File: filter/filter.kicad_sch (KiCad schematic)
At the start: 38 parts, among them Q1 PNP, Q2 PNP, SW1 High Pass / Low Pass, U1 LM13700, U2 TL074, U3 TL072

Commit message: Experiment with pcb
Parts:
- C1, C2, C3, C4, C5, C6: footprint (none) -> Capacitor_THT:C_Disc_D5.0mm_W2.5mm_P2.50mm
- CVLevel1: renamed from CVLevel; footprint (none) -> Potentiometer_THT:Potentiometer_Piher_T-16H_Single_Horizontal
- Cutoff1: renamed from Cutoff; footprint (none) -> Potentiometer_THT:Potentiometer_Piher_T-16H_Single_Horizontal
- D1, D2: footprint (none) -> LED_THT:LED_D5.0mm
- Q1, Q2: footprint (none) -> Package_TO_SOT_THT:TO-92
- R1, R10, R11, R12, R13, R14, R15, R16, R18, R19, R2, R20, R21, R3, R4, R5, R6, R7, R8, R9: footprint (none) -> Resistor_THT:R_Axial_DIN0207_L6.3mm_D2.5mm_P10.16mm_Horizontal
- R17: footprint (none) -> Resistor_THT:R_Axial_DIN0207_L6.3mm_D2.5mm_P2.54mm_Vertical
- Resonance1: renamed from Resonance; footprint (none) -> Potentiometer_THT:Potentiometer_Piher_T-16L_Single_Vertical_Hole
- U1: footprint (none) -> Package_DIP:DIP-16_W7.62mm
- U2: footprint (none) -> Package_DIP:DIP-14_W7.62mm
- U3: footprint (none) -> Package_DIP:DIP-8_W7.62mm
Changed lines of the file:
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@@
 			)
 		)
-		(property "Footprint" ""
+		(property "Footprint" "Resistor_THT:R_Axial_DIN0207_L6.3mm_D2.5mm_P10.16mm_Horizontal"
 			(at 130.556 167.386 90)
 			(effects
@@
 			)
 		)
-		(property "Footprint" ""
+		(property "Footprint" "Package_TO_SOT_THT:TO-92"
 			(at 229.87 82.55 0)
 			(effects
@@
 			)
 		)
-		(property "Footprint" ""
+		(property "Footprint" "Resistor_THT:R_Axial_DIN0207_L6.3mm_D2.5mm_P10.16mm_Horizontal"
 			(at 115.316 167.894 90)
 			(effects
@@
 			)
 		)
-		(property "Footprint" ""
+		(property "Footprint" "Resistor_THT:R_Axial_DIN0207_L6.3mm_D2.5mm_P10.16mm_Horizontal"
 			(at 138.176 72.136 90)
 			(effects
@@
 			)
 		)
-		(property "Footprint" ""
+		(property "Footprint" "Capacitor_THT:C_Disc_D5.0mm_W2.5mm_P2.50mm"
 			(at 29.21 120.65 0)
 			(effects
@@
 			)
 		)
-		(property "Footprint" ""
+		(property "Footprint" "Package_DIP:DIP-16_W7.62mm"
 			(at 33.655 60.96 0)
 			(effects
@@
 			)
 		)
-		(property "Footprint" ""
+		(property "Footprint" "Package_DIP:DIP-8_W7.62mm"
 			(at 25.4 185.42 0)
 			(effects
@@
 			)
 		)
-		(property "Footprint" ""
+		(property "Footprint" "Resistor_THT:R_Axial_DIN0207_L6.3mm_D2.5mm_P10.16mm_Horizontal"
 			(at 115.316 145.034 90)
 			(effects
@@
 			)
 		)
-		(property "Footprint" ""
+		(property "Footprint" "Package_DIP:DIP-8_W7.62mm"
 			(at 33.02 138.43 0)
 			(effects
@@
 			)
 		)
-		(property "Footprint" ""
+		(property "Footprint" "Resistor_THT:R_Axial_DIN0207_L6.3mm_D2.5mm_P10.16mm_Horizontal"
 			(at 81.3435 85.7885 90)
 			(effects
@@
 			)
 		)
-		(property "Footprint" ""
+		(property "Footprint" "Resistor_THT:R_Axial_DIN0207_L6.3mm_D2.5mm_P10.16mm_Horizontal"
 			(at 220.726 106.426 90)
 			(effects
@@
 			)
 		)
-		(property "Footprint" ""
+		(property "Footprint" "Package_DIP:DIP-16_W7.62mm"
 			(at 204.47 55.245 0)
 			(effects
@@
 			)
 		)
-		(property "Footprint" ""
+		(property "Footprint" "Resistor_THT:R_Axial_DIN0207_L6.3mm_D2.5mm_P10.16mm_Horizontal"
 			(at 192.024 66.294 90)
 			(effects
@@
 		(exclude_from_sim no)
 		(in_bom yes)
-		(on_board yes)
+		(on_board no)
 		(dnp no)
 		(property "Reference" "R17"
@@
 			)
 		)
-		(property "Footprint" ""
+		(property "Footprint" "Resistor_THT:R_Axial_DIN0207_L6.3mm_D2.5mm_P2.54mm_Vertical"
 			(at 73.406 48.006 90)
 			(effects
@@
 			)
 		)
-		(property "Footprint" ""
+		(property "Footprint" "Capacitor_THT:C_Disc_D5.0mm_W2.5mm_P2.50mm"
 			(at 39.37 120.65 0)
 			(effects
@@
 		(exclude_from_sim no)
 		(in_bom yes)
-		(on_board yes)
+		(on_board no)
 		(dnp no)
-		(property "Reference" "Resonance"
+		(property "Reference" "Resonance1"
 			(at 113.792 40.64 90)
 			(effects
@@
 			)
 		)
-		(property "Footprint" ""
+		(property "Footprint" "Potentiometer_THT:Potentiometer_Piher_T-16L_Single_Vertical_Hole"
 			(at 118.11 44.45 0)
 			(effects
@@
 			(project "low-pass-filter"
 				(path "/e72ee090-6f9b-4823-9ab6-f31beee51bd1"
-					(reference "Resonance")
+					(reference "Resonance1")
 					(unit 1)
 				)
@@
 			)
 		)
-		(property "Footprint" ""
+		(property "Footprint" "Resistor_THT:R_Axial_DIN0207_L6.3mm_D2.5mm_P10.16mm_Horizontal"
 			(at 260.604 114.554 90)
 			(effects
@@
 			)
 		)
-		(property "Footprint" ""
+		(property "Footprint" "Capacitor_THT:C_Disc_D5.0mm_W2.5mm_P2.50mm"
 			(at 243.84 95.25 0)
 			(effects
@@
 			)
 		)
-		(property "Footprint" ""
+		(property "Footprint" "Capacitor_THT:C_Disc_D5.0mm_W2.5mm_P2.50mm"
 			(at 237.49 40.64 0)
 			(effects
@@
 			)
 		)
-		(property "Footprint" ""
+		(property "Footprint" "LED_THT:LED_D5.0mm"
 			(at 137.16 97.79 0)
 			(effects
@@
 			)
 		)
-		(property "Footprint" ""
+		(property "Footprint" "Resistor_THT:R_Axial_DIN0207_L6.3mm_D2.5mm_P10.16mm_Horizontal"
 			(at 233.934 141.986 90)
 			(effects
@@
 			)
 		)
-		(property "Footprint" ""
+		(property "Footprint" "Resistor_THT:R_Axial_DIN0207_L6.3mm_D2.5mm_P10.16mm_Horizontal"
 			(at 192.024 43.434 90)
 			(effects
@@
 			)
 		)
-		(property "Footprint" ""
+		(property "Footprint" "Resistor_THT:R_Axial_DIN0207_L6.3mm_D2.5mm_P10.16mm_Horizontal"
 			(at 220.726 123.444 90)
 			(effects
@@
 			)
 		)
-		(property "Footprint" ""
+		(property "Footprint" "Package_DIP:DIP-14_W7.62mm"
 			(at 207.01 27.94 0)
 			(effects
@@
 			)
 		)
-		(property "Footprint" ""
+		(property "Footprint" "Package_DIP:DIP-14_W7.62mm"
 			(at 245.11 81.28 0)
 			(effects
@@
 			)
 		)
-		(property "Footprint" ""
+		(property "Footprint" "Resistor_THT:R_Axial_DIN0207_L6.3mm_D2.5mm_P10.16mm_Horizontal"
 			(at 242.824 147.574 90)
 			(effects
@@
 			)
 		)
-		(property "Footprint" ""
+		(property "Footprint" "Resistor_THT:R_Axial_DIN0207_L6.3mm_D2.5mm_P10.16mm_Horizontal"
 			(at 105.156 155.956 90)
 			(effects
@@
 			)
 		)
-		(property "Footprint" ""
+		(property "Footprint" "Resistor_THT:R_Axial_DIN0207_L6.3mm_D2.5mm_P10.16mm_Horizontal"
 			(at 235.204 106.426 90)
 			(effects
@@
 		(exclude_from_sim no)
 		(in_bom yes)
-		(on_board yes)
+		(on_board no)
 		(dnp no)
-		(property "Reference" "CVLevel"
+		(property "Reference" "CVLevel1"
 			(at 212.598 139.7 0)
 			(effects
@@
 			)
 		)
-		(property "Footprint" ""
+		(property "Footprint" "Potentiometer_THT:Potentiometer_Piher_T-16H_Single_Horizontal"
 			(at 214.63 140.97 0)
 			(effects
@@
 			(project "low-pass-filter"
 				(path "/e72ee090-6f9b-4823-9ab6-f31beee51bd1"
-					(reference "CVLevel")
+					(reference "CVLevel1")
 					(unit 1)
 				)
@@
 			)
 		)
-		(property "Footprint" ""
+		(property "Footprint" "Capacitor_THT:C_Disc_D5.0mm_W2.5mm_P2.50mm"
 			(at 154.94 44.45 0)
 			(effects
@@
 			)
 		)
-		(property "Footprint" ""
+		(property "Footprint" "Package_DIP:DIP-16_W7.62mm"
 			(at 29.21 84.455 0)
 			(effects
@@
 		(exclude_from_sim no)
 		(in_bom yes)
-		(on_board yes)
+		(on_board no)
 		(dnp no)
 		(fields_autoplaced yes)
@@
 		(exclude_from_sim no)
 		(in_bom yes)
-		(on_board yes)
+		(on_board no)
 		(dnp no)
-		(property "Reference" "Cutoff"
+		(property "Reference" "Cutoff1"
 			(at 243.84 159.258 90)
 			(effects
@@
 			)
 		)
-		(property "Footprint" ""
+		(property "Footprint" "Potentiometer_THT:Potentiometer_Piher_T-16H_Single_Horizontal"
 			(at 243.84 156.21 0)
 			(effects
@@
 			(project "low-pass-filter"
 				(path "/e72ee090-6f9b-4823-9ab6-f31beee51bd1"
-					(reference "Cutoff")
+					(reference "Cutoff1")
 					(unit 1)
 				)
@@
 			)
 		)
-		(property "Footprint" ""
+		(property "Footprint" "Package_DIP:DIP-14_W7.62mm"
 			(at 30.48 49.53 0)
 			(effects
@@
 			)
 		)
-		(property "Footprint" ""
+		(property "Footprint" "Resistor_THT:R_Axial_DIN0207_L6.3mm_D2.5mm_P10.16mm_Horizontal"
 			(at 98.806 98.044 90)
 			(effects
@@
 			)
 		)
-		(property "Footprint" ""
+		(property "Footprint" "Package_DIP:DIP-14_W7.62mm"
 			(at 134.62 130.81 0)
 			(effects
@@
 			)
 		)
-		(property "Footprint" ""
+		(property "Footprint" "Package_DIP:DIP-16_W7.62mm"
 			(at 29.21 103.505 0)
 			(effects
@@
 			)
 		)
-		(property "Footprint" ""
+		(property "Footprint" "Package_DIP:DIP-8_W7.62mm"
 			(at 82.55 93.98 0)
 			(effects
@@
 			)
 		)
-		(property "Footprint" ""
+		(property "Footprint" "Package_TO_SOT_THT:TO-92"
 			(at 243.84 82.55 0)
 			(effects
@@
 			)
 		)
-		(property "Footprint" ""
+		(property "Footprint" "Resistor_THT:R_Axial_DIN0207_L6.3mm_D2.5mm_P10.16mm_Horizontal"
 			(at 176.276 45.466 90)
 			(effects
@@
 			)
 		)
-		(property "Footprint" ""
+		(property "Footprint" "Package_DIP:DIP-14_W7.62mm"
 			(at 139.7 53.34 0)
 			(effects
@@
 			)
 		)
-		(property "Footprint" ""
+		(property "Footprint" "LED_THT:LED_D5.0mm"
 			(at 138.43 83.82 0)
 			(effects
@@
 			)
 		)
-		(property "Footprint" ""
+		(property "Footprint" "Package_DIP:DIP-16_W7.62mm"
 			(at 129.54 156.845 0)
 			(effects
@@
 			)
 		)
-		(property "Footprint" ""
+		(property "Footprint" "Resistor_THT:R_Axial_DIN0207_L6.3mm_D2.5mm_P10.16mm_Horizontal"
 			(at 176.784 66.294 90)
 			(effects
@@
 			)
 		)
-		(property "Footprint" ""
+		(property "Footprint" "Capacitor_THT:C_Disc_D5.0mm_W2.5mm_P2.50mm"
 			(at 149.86 104.14 0)
 			(effects
@@
 			)
 		)
-		(property "Footprint" ""
+		(property "Footprint" "Resistor_THT:R_Axial_DIN0207_L6.3mm_D2.5mm_P10.16mm_Horizontal"
 			(at 98.806 85.344 90)
 			(effects
@@
 			)
 		)
-		(property "Footprint" ""
+		(property "Footprint" "Resistor_THT:R_Axial_DIN0207_L6.3mm_D2.5mm_P10.16mm_Horizontal"
 			(at 252.476 139.954 90)
 			(effects
@@
 			)
 		)
-		(property "Footprint" ""
+		(property "Footprint" "Resistor_THT:R_Axial_DIN0207_L6.3mm_D2.5mm_P10.16mm_Horizontal"
 			(at 119.126 59.436 90)
 			(effects

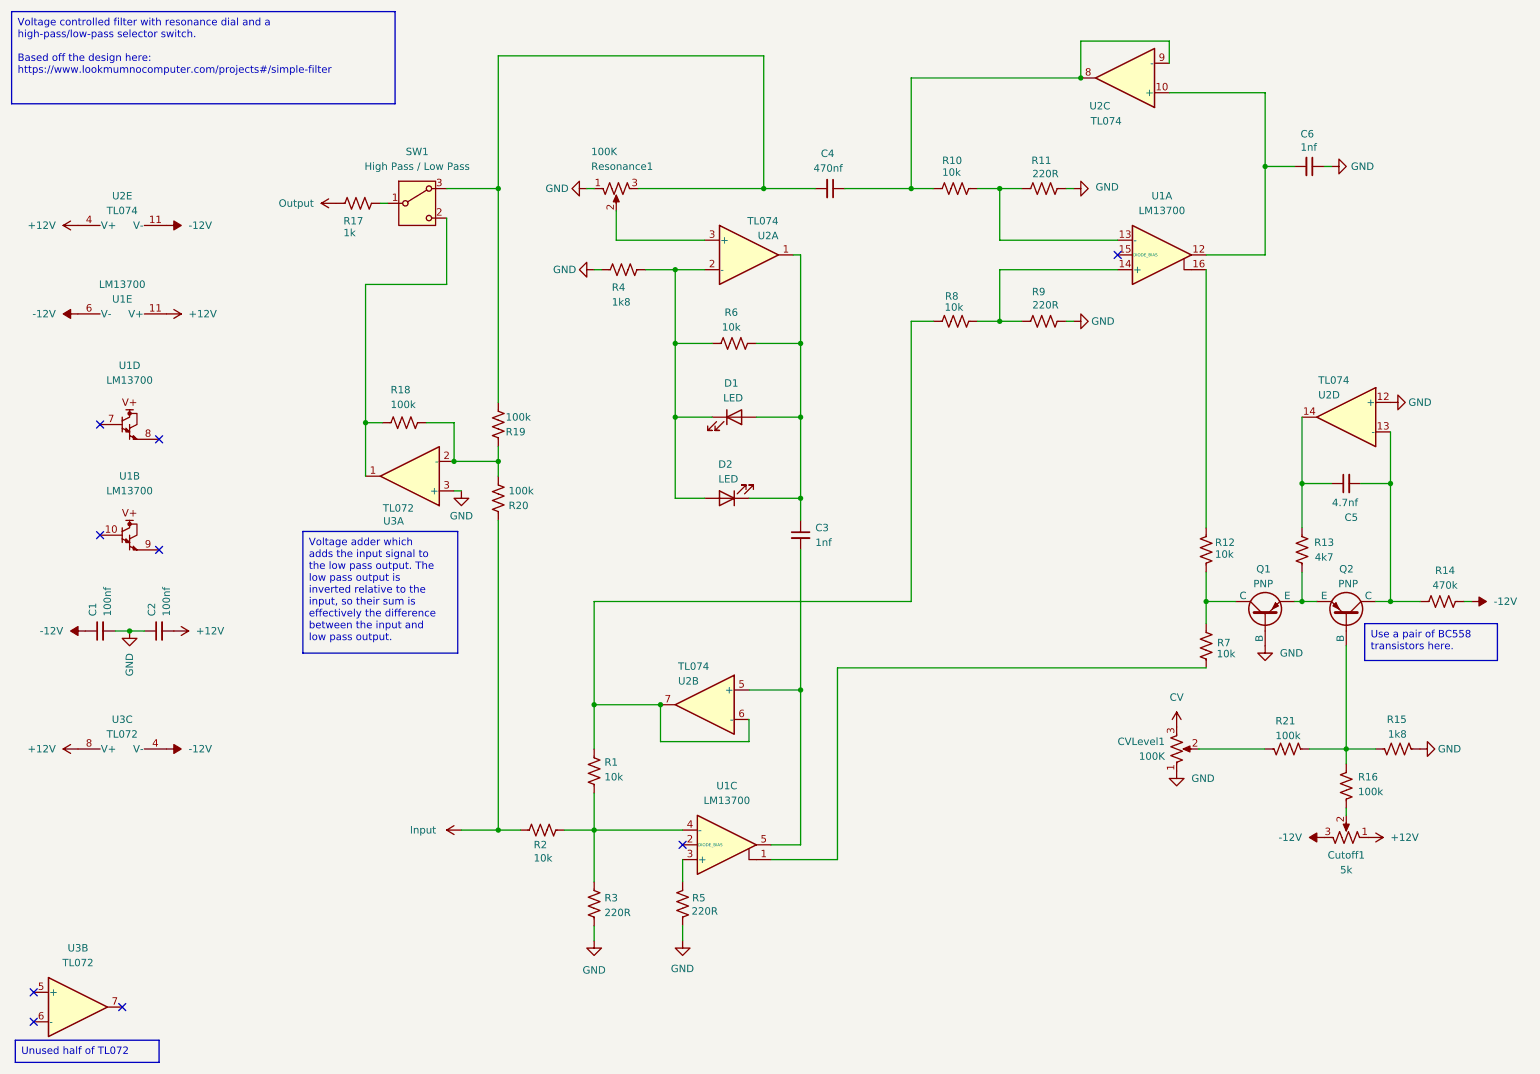
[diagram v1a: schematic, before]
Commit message: Remove high-pass filter switch from filter
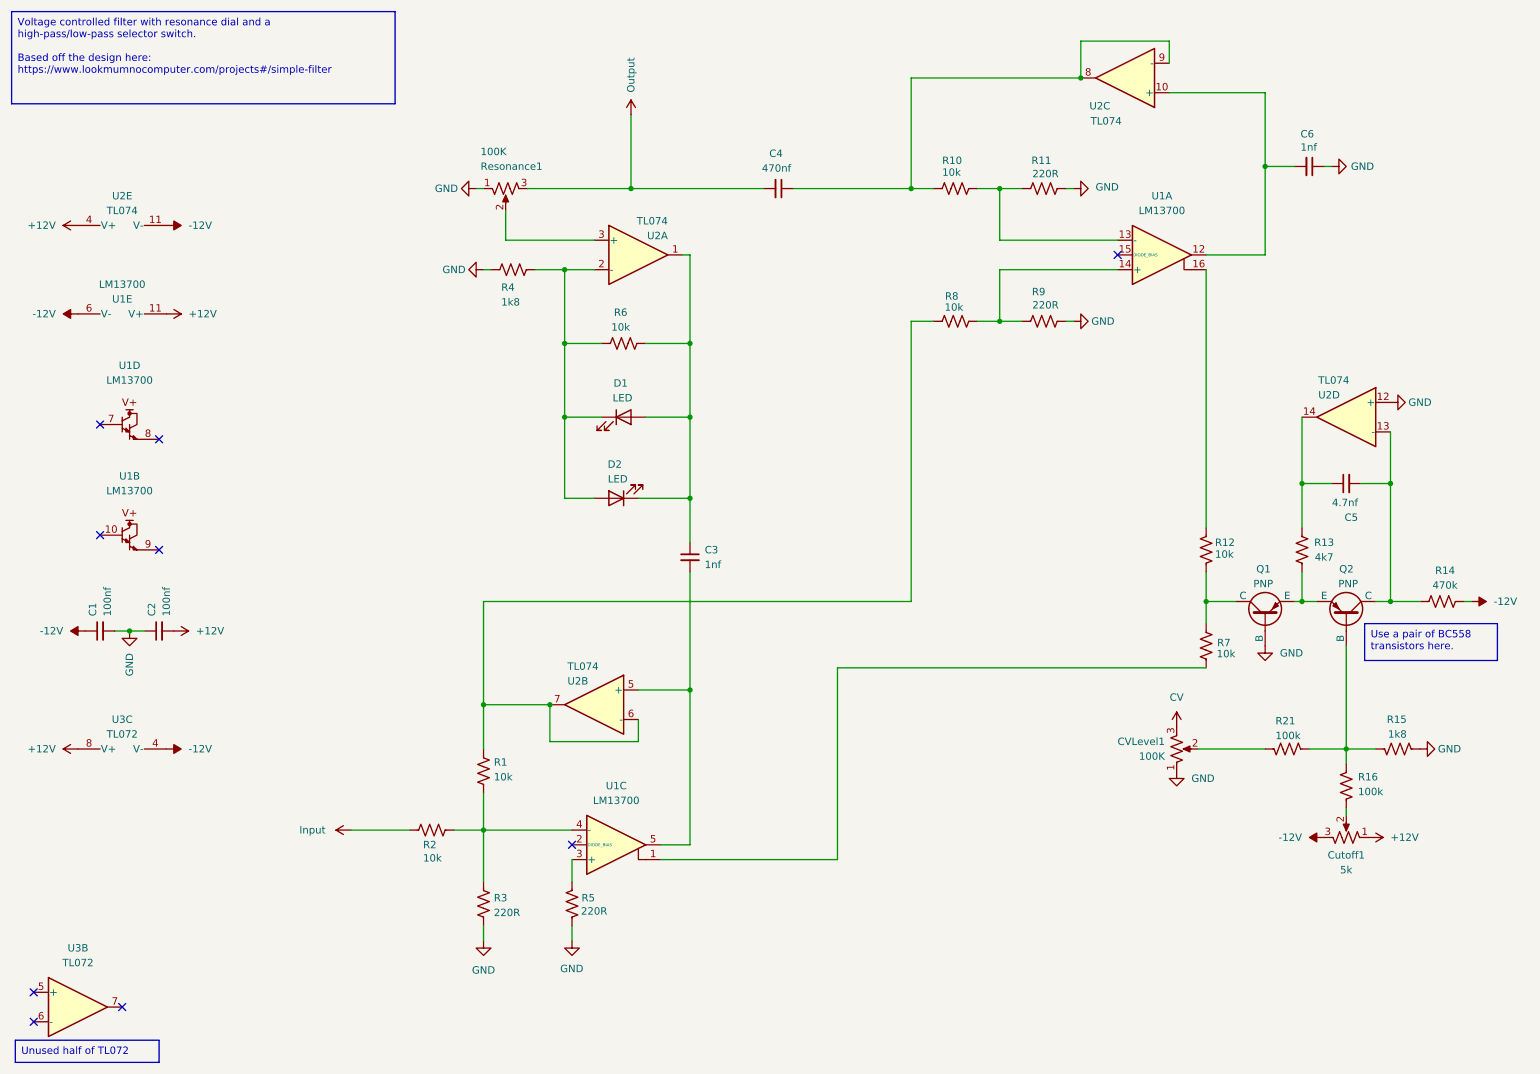
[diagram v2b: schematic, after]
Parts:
- removed R17: 1k, Resistor_THT:R_Axial_DIN0207_L6.3mm_D2.5mm_P2.54mm_Vertical, symbol Device:R_US
- removed R18, R19, R20: 100k, Resistor_THT:R_Axial_DIN0207_L6.3mm_D2.5mm_P10.16mm_Horizontal, symbol Device:R_US
- removed SW1: High Pass / Low Pass, symbol Switch:SW_SPDT_312
- removed unit 1 of U3
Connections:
- net Output: now also C4.2, Resonance1.3
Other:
- moved on the sheet: C3, C4, D1, D2, R1, R2, R3, R4, R5, R6, Resonance1, U1C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
